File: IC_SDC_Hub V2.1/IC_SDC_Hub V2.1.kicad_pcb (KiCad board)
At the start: 2 copper layers, 58 x 78 mm, 33 parts, among them J1 JST-XA, J2 JST-XA, J3 JST-XA, J4 JST-XA, J5 JST-XA, J6 JST-XA, J8 Conn_01x03, J9 Conn_01x03, Q1 BSS205N, Q2 BSS205N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

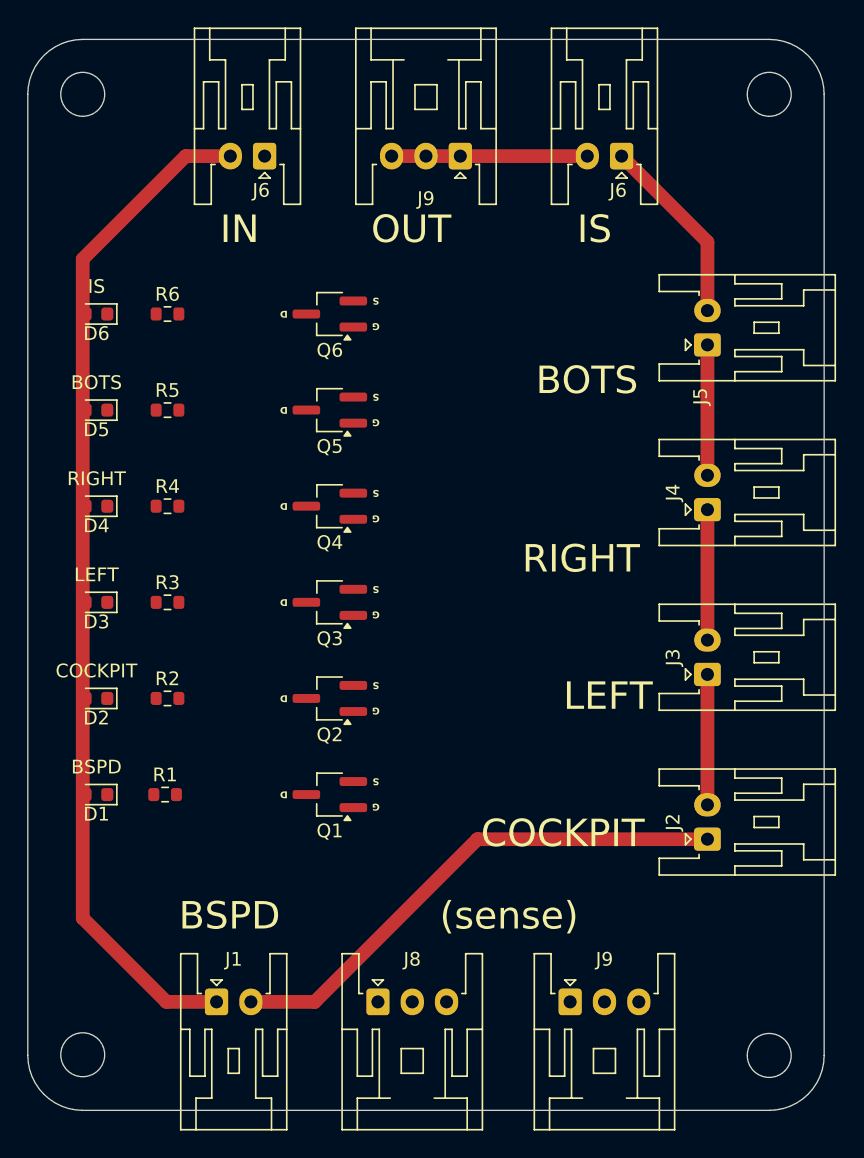
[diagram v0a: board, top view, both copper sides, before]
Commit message: Add files via upload
PCB routing done.
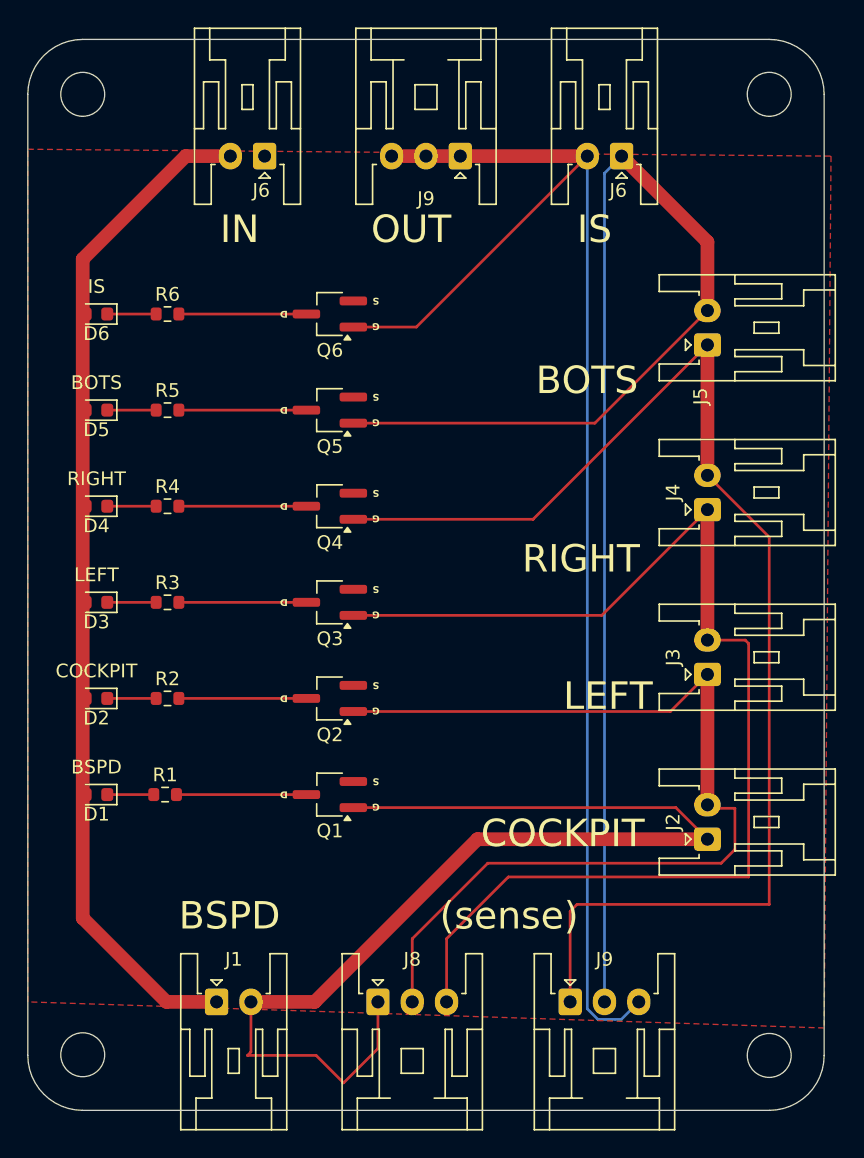
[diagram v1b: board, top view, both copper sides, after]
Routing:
- net BOTS_OK: track 13.8 -> 105.1 mm
- net IS_OK: track 14.2 -> 103.1 mm
- net R_OK: track 9.50 -> 95.0 mm
- net L_OK: track 9.50 -> 87.0 mm
- net CK_OK: track 9.50 -> 72.3 mm
- net BSPD_OK: track 38.2 -> 83.7 mm
- net Net-(Q2-D): track 0.00 -> 9.47 mm
- net Net-(Q7-D): track 0.00 -> 9.29 mm
- net Net-(Q6-D): track 0.00 -> 9.29 mm
- net Net-(Q5-D): track 0.00 -> 9.29 mm
- net Net-(Q4-D): track 0.00 -> 9.29 mm
- net Net-(Q3-D): track 0.00 -> 9.29 mm
- net Net-(D7-K): track 0.00 -> 3.56 mm
- net Net-(D6-K): track 0.00 -> 3.56 mm
- net Net-(D5-K): track 0.00 -> 3.56 mm
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- added copper zone on F.Cu, net GND

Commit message: Final mods
made small changes to routing 
expanded ground plane
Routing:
- net IS_OK: track 103.1 -> 120.0 mm
- net BOTS_OK: track 105.1 -> 111.1 mm
- net R_OK: track 95.0 -> 92.9 mm
- net CK_OK: track 72.3 -> 71.4 mm
- added copper zone on B.Cu, net GND
